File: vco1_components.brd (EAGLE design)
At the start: 106 x 50 mm, 59 parts, among them IC1 LM13700N, Q3 2N3904, Q4 2N3904, U1 TL072_, U2 TL072_, U3 TL072_

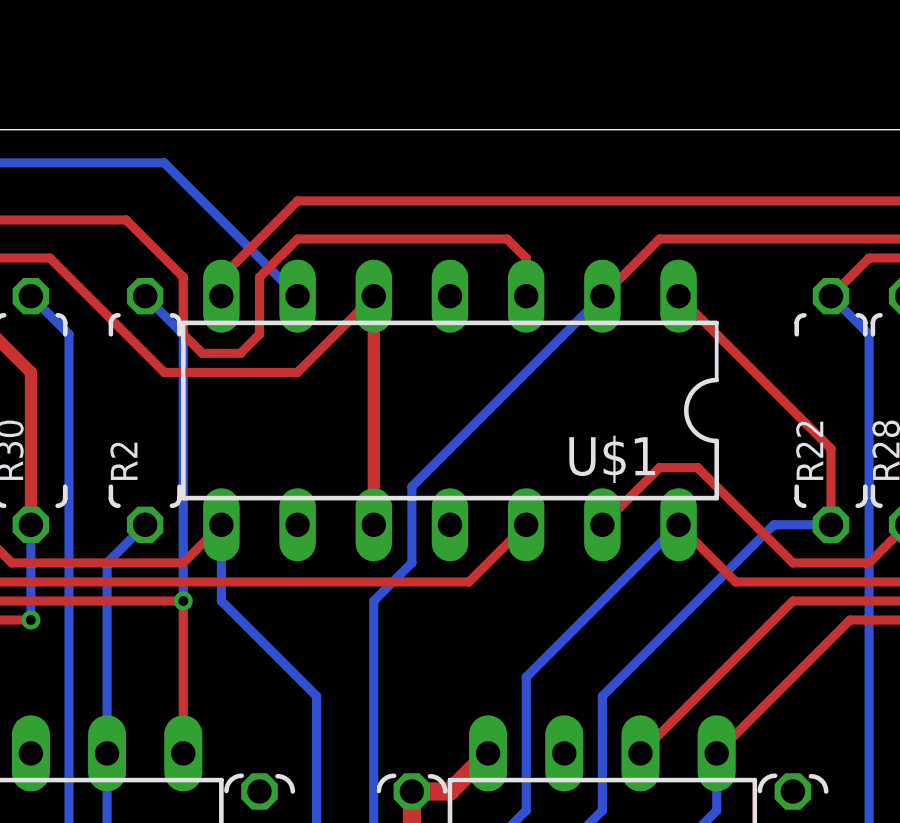
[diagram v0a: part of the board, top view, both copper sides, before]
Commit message: Transistor outlines on THAT 340
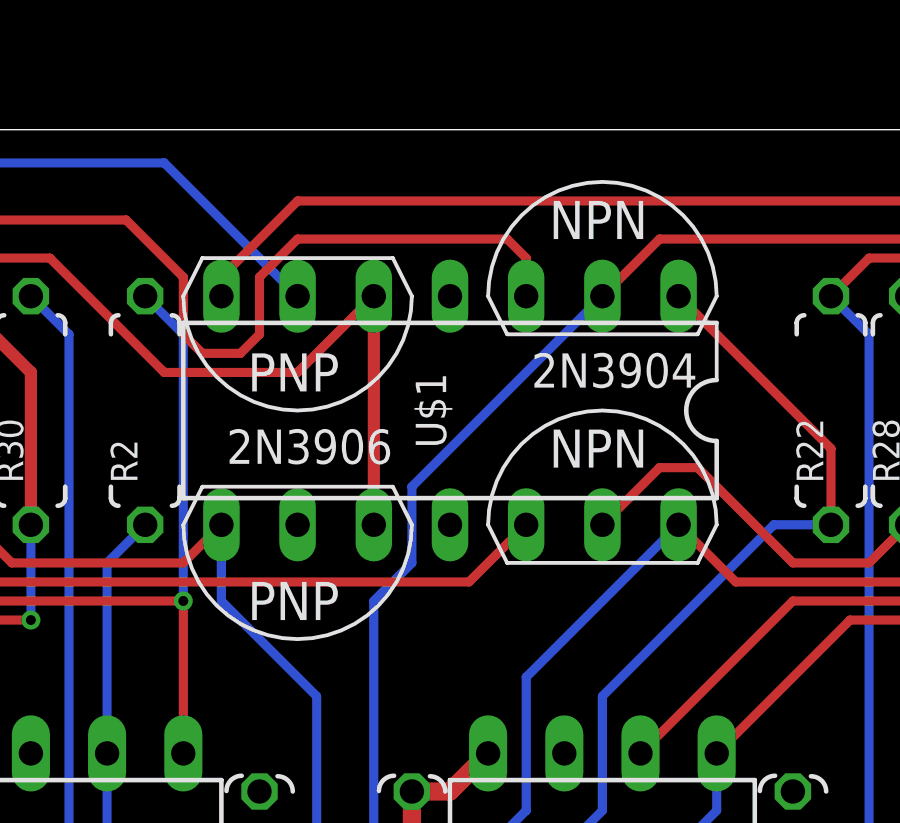
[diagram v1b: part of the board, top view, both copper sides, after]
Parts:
- U$1: value THAT-340 -> THAT-340TRANSISTORS; device MusicThingModular:DIL14 -> MusicThingModular:THAT340
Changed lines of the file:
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@@
 <element name="U3" library="MusicThingModular" package="DIL08" value="TL072_" x="30.48" y="25.4" rot="R180"/>
 <element name="V/OCT_TRIM" library="MusicThingModular" package="BOURNS_3362P_TRIMMER" value="100R" x="15.24" y="44.45" rot="MR0"/>
-<element name="U$1" library="MusicThingModular" package="DIL14" value="THAT-340" x="60.96" y="40.64" rot="R180"/>
+<element name="U$1" library="MusicThingModular" package="THAT340" value="THAT-340TRANSISTORS" x="60.96" y="40.64" rot="R180"/>
 <element name="SV1" library="MusicThingModular" package="EURO_PWR_HEADER_LOCK" value="EURO_POWER_HEADERLOCK_PADS" x="8.89" y="25.4" rot="MR180"/>
 <element name="C6" library="SparkFun-Passives" package="CPOL-RADIAL-10UF-25V" value="10uf" x="17.78" y="20.32" rot="R90"/>
